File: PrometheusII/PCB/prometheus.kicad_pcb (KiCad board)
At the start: 4 copper layers, 223.5 x 222.3 mm, 240 parts, among them J1 0878311420, J10 Conn_02x02_Odd_Even, J11 Conn_02x02_Odd_Even, J12 Conn_02x08_Odd_Even, J13 Conn_02x08_Odd_Even, J14 Conn_02x08_Odd_Even, J2 Conn_02x08_Odd_Even, J3 Conn_02x02_Odd_Even, J4 Conn_02x02_Odd_Even, J7 Conn_02x08_Odd_Even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

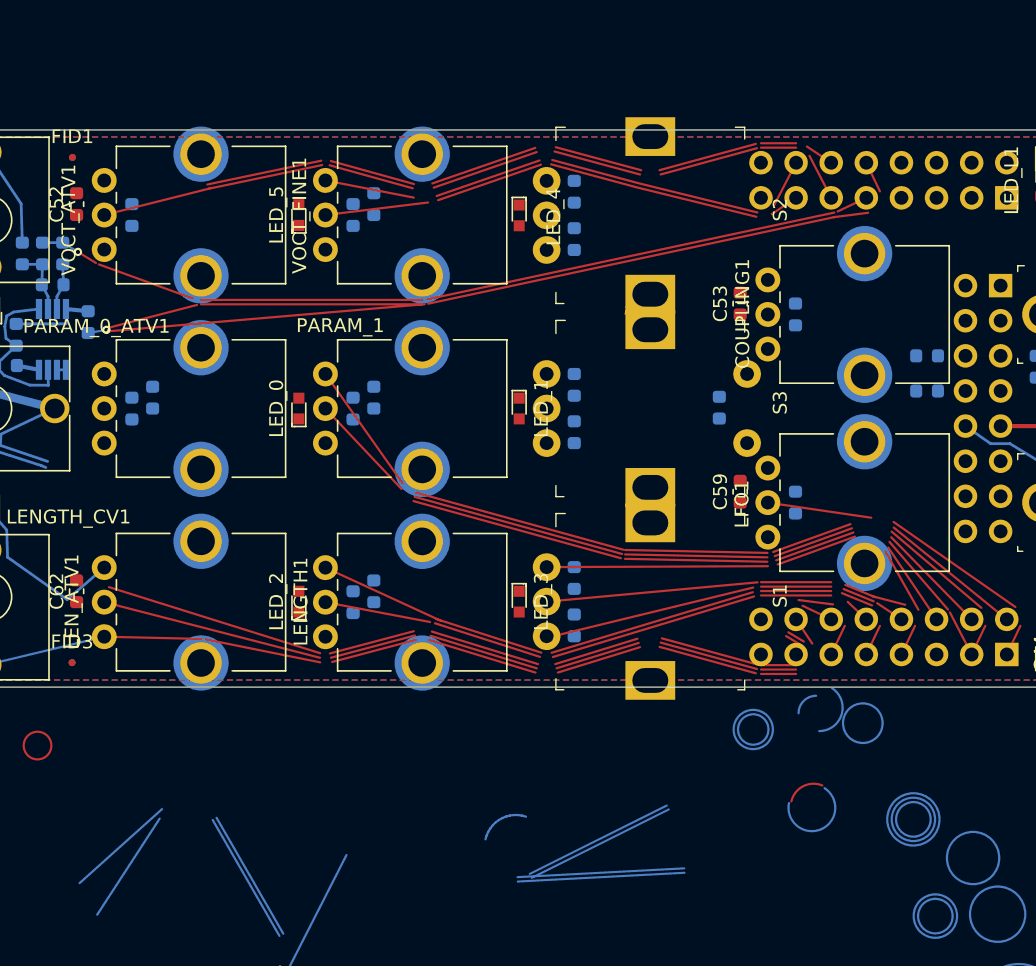
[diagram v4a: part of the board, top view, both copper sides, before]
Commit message: Updated arc completion to merge nets
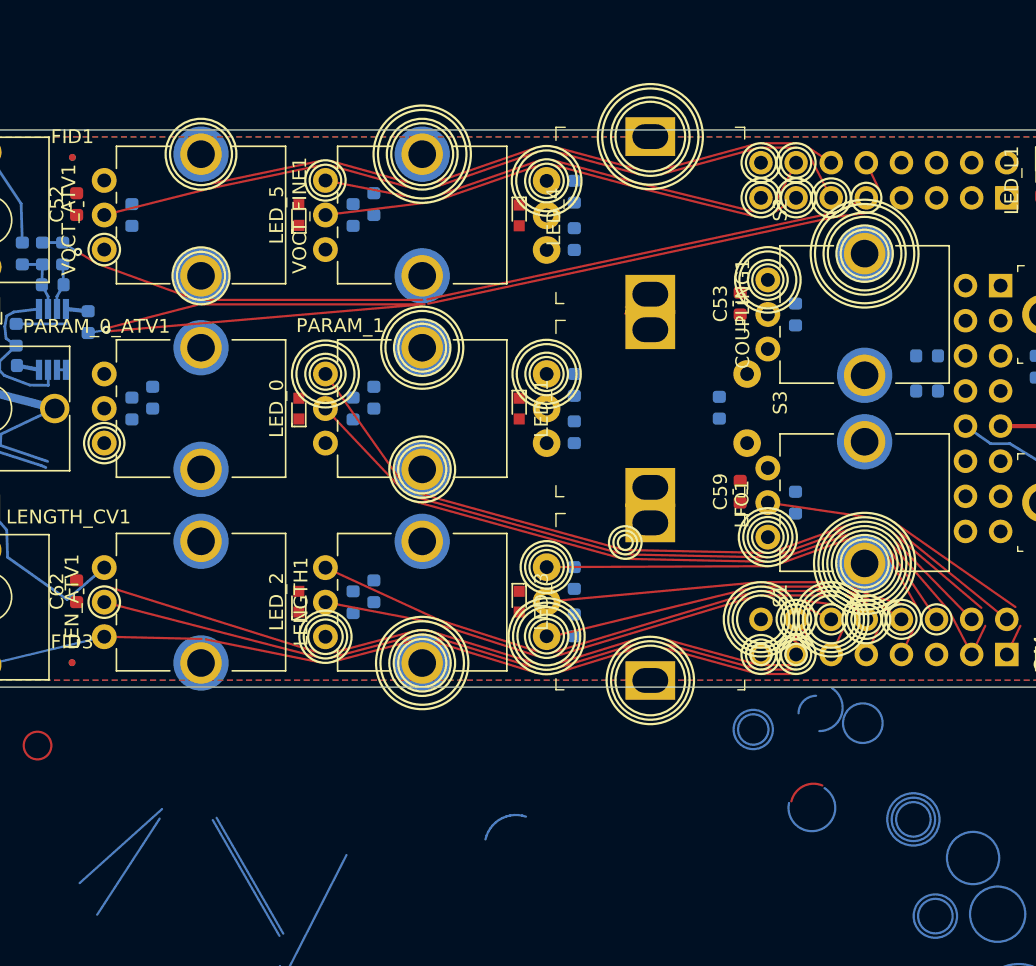
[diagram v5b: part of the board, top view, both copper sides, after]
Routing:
- net (no net): track 418.6 -> 372.2 mm
- net GND: track 539.3 -> 540.6 mm
- net /LEN_ATV_P: track 50.0 -> 51.2 mm
- net /LEN_CV_P: track 59.4 -> 60.4 mm

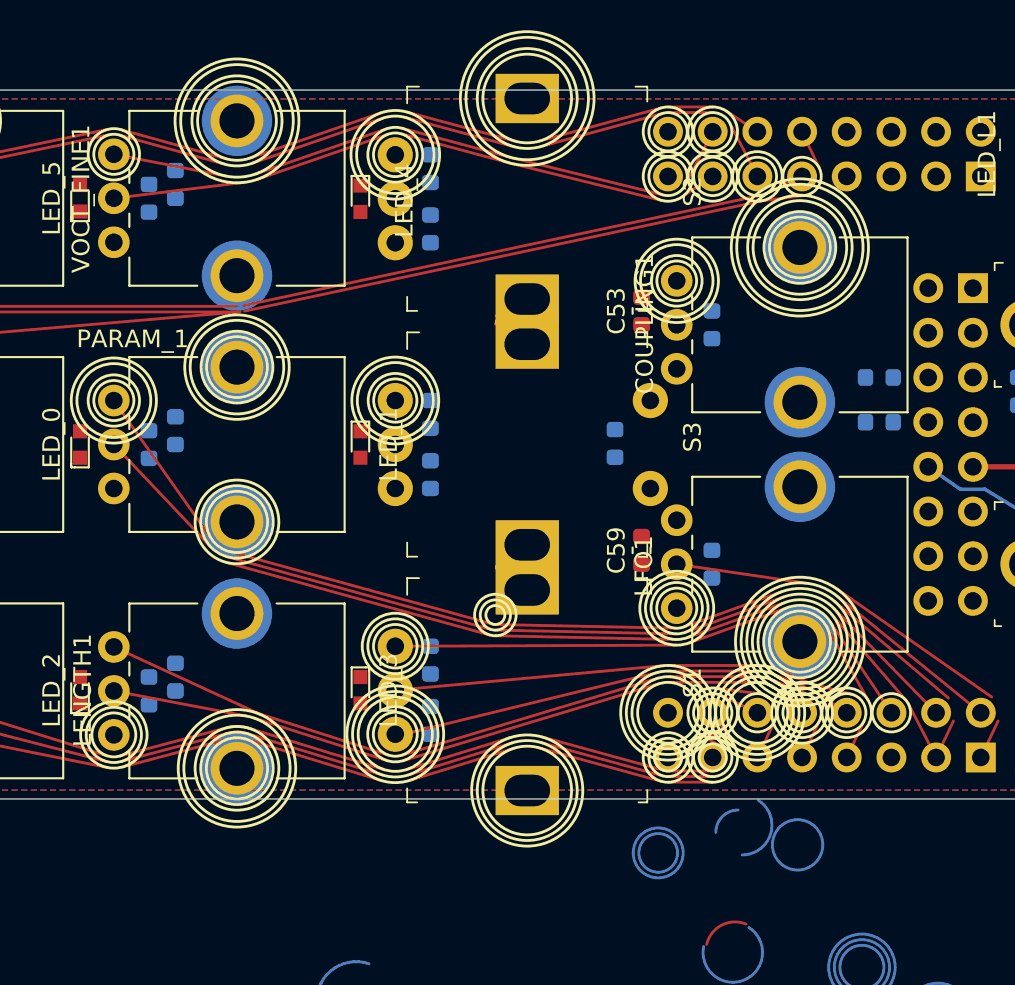
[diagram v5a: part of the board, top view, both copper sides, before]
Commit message: Some routing with arc completion
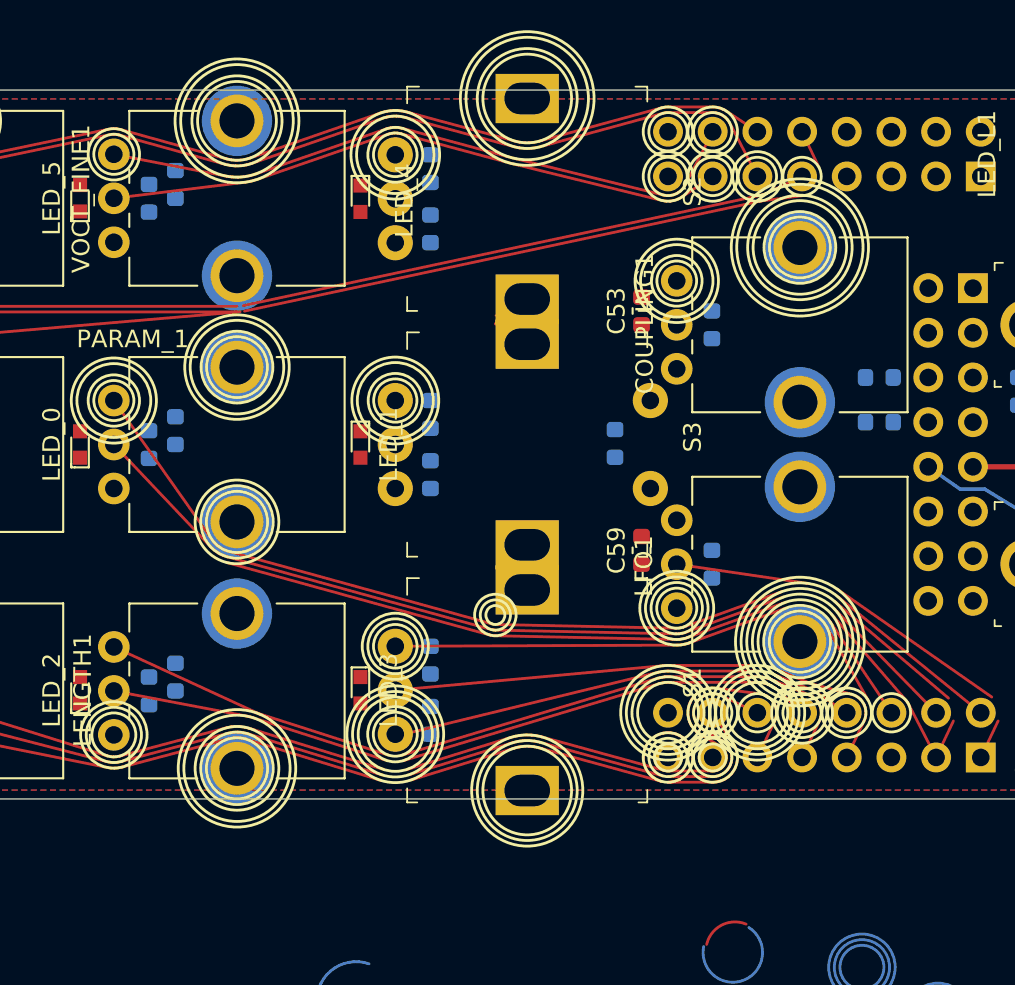
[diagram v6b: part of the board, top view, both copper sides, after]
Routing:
- net GND: track 540.6 -> 633.4 mm
- net (no net): track 372.2 -> 329.2 mm
- net /LEN_KNOB_P: track 9.55 -> 40.0 mm
- net /LEN_CV_P: track 60.4 -> 45.3 mm
- net /LEN_ATV_P: track 51.2 -> 39.3 mm
- net /VOCT_ATV_P: track 50.0 -> 56.4 mm
- net /VOCT_FINE_P: track 32.7 -> 35.4 mm
- net /PARAM_1_P: track 48.1 -> 50.0 mm
- net /VOCT_OCT_A_P: track 28.2 -> 28.9 mm
- net /VOCT_OCT_B_P: track 24.7 -> 25.2 mm

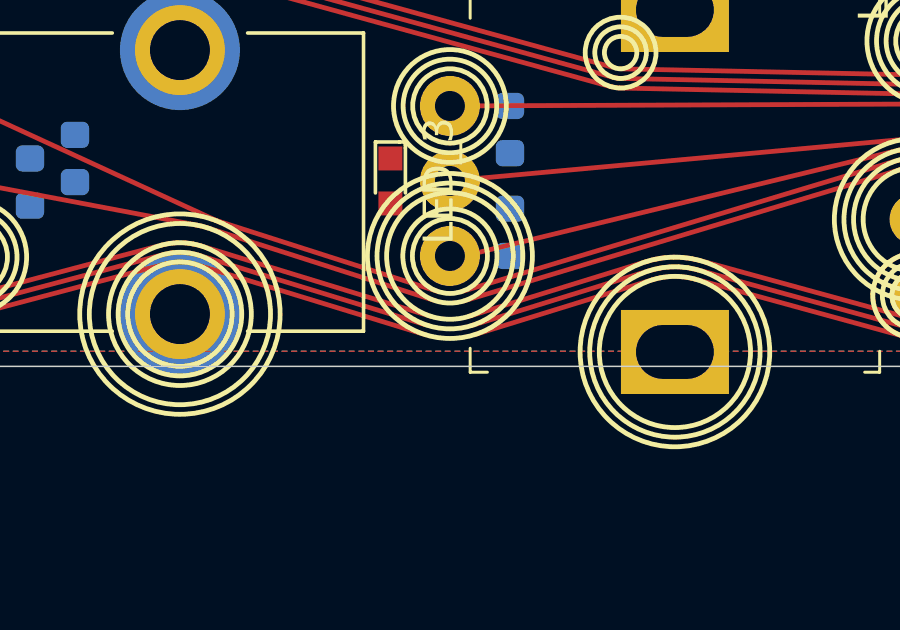
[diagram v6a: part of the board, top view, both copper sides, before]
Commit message: Fixed arc orientation issue
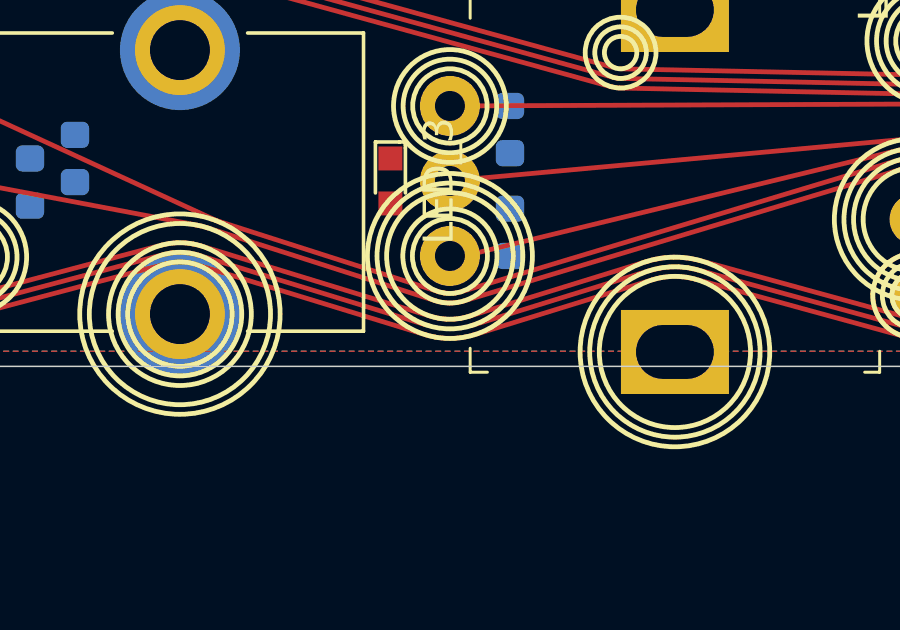
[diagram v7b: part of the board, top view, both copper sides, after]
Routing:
- net GND: track 633.4 -> 635.5 mm
- net (no net): track 329.2 -> 330.8 mm
- net /LEN_KNOB_P: track 40.0 -> 40.9 mm
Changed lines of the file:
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@@
     (thickness 1.6)
     (drawings 246)
-    (tracks 1001)
+    (tracks 1019)
     (zones 0)
     (modules 240)
@@
   (segment (start 85.410827 120.09175) (end 85.264931 120.079665) (width 0.16) (layer F.Cu) (net 0))
   (segment (start 85.264931 120.079665) (end 85.121654 120.049608) (width 0.16) (layer F.Cu) (net 0))
+  (segment (start 78.939684 128.319288) (end 79.25855 128.396544) (width 0.16) (layer F.Cu) (net 0))
+  (segment (start 79.25855 128.396544) (end 79.584349 128.435274) (width 0.16) (layer F.Cu) (net 0))
+  (segment (start 79.584349 128.435274) (end 79.912441 128.434928) (width 0.16) (layer F.Cu) (net 0))
+  (segment (start 79.912441 128.434928) (end 80.238156 128.39551) (width 0.16) (layer F.Cu) (net 0))
+  (segment (start 80.238156 128.39551) (end 80.55686 128.317583) (width 0.16) (layer F.Cu) (net 0))
   (segment (start 95.25 122.74) (end 94.998028 122.758447) (width 0.16) (layer F.Cu) (net 80))
   (segment (start 94.998028 122.758447) (end 94.751431 122.813398) (width 0.16) (layer F.Cu) (net 80))
@@
   (segment (start 95.402371 95.059297) (end 95.195043 95.068613) (width 0.16) (layer F.Cu) (net 1))
   (segment (start 95.195043 95.068613) (end 94.989706 95.038464) (width 0.16) (layer F.Cu) (net 1))
+  (segment (start 79.127218 127.707381) (end 79.371876 127.766657) (width 0.16) (layer F.Cu) (net 1))
+  (segment (start 79.371876 127.766657) (end 79.621852 127.796373) (width 0.16) (layer F.Cu) (net 1))
+  (segment (start 79.621852 127.796373) (end 79.873588 127.796108) (width 0.16) (layer F.Cu) (net 1))
+  (segment (start 79.873588 127.796108) (end 80.123501 127.765864) (width 0.16) (layer F.Cu) (net 1))
+  (segment (start 80.123501 127.765864) (end 80.368034 127.706073) (width 0.16) (layer F.Cu) (net 1))
+  (segment (start 79.364324 126.880464) (end 79.547188 126.924168) (width 0.16) (layer F.Cu) (net 1))
+  (segment (start 79.547188 126.924168) (end 79.734537 126.939951) (width 0.16) (layer F.Cu) (net 1))
+  (segment (start 79.734537 126.939951) (end 79.922135 126.927457) (width 0.16) (layer F.Cu) (net 1))
+  (segment (start 79.922135 126.927457) (end 80.105737 126.886966) (width 0.16) (layer F.Cu) (net 1))
   (segment (start 100.557255 95.046046) (end 100.679887 95.012317) (width 0.16) (layer F.Cu) (net 72))
   (segment (start 100.679887 95.012317) (end 100.797755 94.964532) (width 0.16) (layer F.Cu) (net 72))
@@
   (segment (start 101.08684 122.914335) (end 101.312144 123.045818) (width 0.16) (layer F.Cu) (net 80))
   (segment (start 101.312144 123.045818) (end 101.515117 123.209684) (width 0.16) (layer F.Cu) (net 80))
+  (segment (start 79.266743 127.185223) (end 79.49642 127.240115) (width 0.16) (layer F.Cu) (net 80))
+  (segment (start 79.49642 127.240115) (end 79.731731 127.259939) (width 0.16) (layer F.Cu) (net 80))
+  (segment (start 79.731731 127.259939) (end 79.967354 127.244246) (width 0.16) (layer F.Cu) (net 80))
+  (segment (start 79.967354 127.244246) (end 80.197958 127.19339) (width 0.16) (layer F.Cu) (net 80))
   (segment (start 96.240825 119.897589) (end 96.069823 119.947635) (width 0.16) (layer F.Cu) (net 85))
   (segment (start 96.069823 119.947635) (end 95.893998 119.976479) (width 0.16) (layer F.Cu) (net 85))
